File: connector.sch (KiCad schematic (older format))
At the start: 16 parts

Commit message: Add vias and ground connections
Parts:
- J301: renamed from J?; footprint (none) -> breakout:SEAM-50-02.0-S-08-2-A-K-TR
- J302: renamed from J?; footprint (none) -> breakout:SEAF-50-05.0-S-08-2-A-K-TR
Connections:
- net GND: now reaches J301.G17, J302.G17
- net GND: now also J301.A28, J301.A3, J301.A37, J301.A4, J301.A40, J301.A43, J301.B14, J301.B3, J301.B31, J301.B38, J301.B4, J301.B41, J301.B44, J301.B47, J301.C21, J301.C24, J301.C27, J301.C3, J301.C30, J301.C33, J301.C36, J301.C39, J301.C4, J301.C42, J301.C45, J301.D20, J301.D23, J301.D26, J301.D29, J301.D32, J301.D35, J301.D38, J301.D41, J301.D44, J301.E19, J301.E22, J301.E25, J301.E28, J301.E31, J301.E34, J301.E37, J301.E40, J301.E43, J301.E46, J301.F10, J301.F15, J301.F21, J301.F24, J301.F27, J301.F30, J301.F33, J301.F36, J301.F39, J301.F42, J301.F45, J301.F49, J301.G20, J301.G23, J301.G26, J301.G29, J301.G3, J301.G32, J301.G35, J301.G38, J301.G41, J301.G44, J301.G47, J301.G50, J301.H19, J301.H22, J301.H25, J301.H28, J301.H31, J301.H34, J301.H37, J301.H40, J301.H43, J301.H46, J301.H49, J302.A28, J302.A3, J302.A37, J302.A4, J302.A40, J302.A43, J302.B14, J302.B3, J302.B31, J302.B38, J302.B4, J302.B41, J302.B44, J302.B47, J302.C21, J302.C24, J302.C27, J302.C3, J302.C30, J302.C33, J302.C36, J302.C39, J302.C4, J302.C42, J302.C45, J302.D20, J302.D23, J302.D26, J302.D29, J302.D32, J302.D35, J302.D38, J302.D41, J302.D44, J302.E19, J302.E22, J302.E25, J302.E28, J302.E31, J302.E34, J302.E37, J302.E40, J302.E43, J302.E46, J302.F10, J302.F15, J302.F21, J302.F24, J302.F27, J302.F30, J302.F33, J302.F36, J302.F39, J302.F42, J302.F45, J302.F49, J302.G20, J302.G23, J302.G26, J302.G29, J302.G3, J302.G32, J302.G35, J302.G38, J302.G41, J302.G44, J302.G47, J302.G50, J302.H19, J302.H22, J302.H25, J302.H28, J302.H31, J302.H34, J302.H37, J302.H40, J302.H43, J302.H46, J302.H49
- new net: J301.C1, J302.C1
- new net: J301.C10, J302.C10
- new net: J301.C11, J302.C11
- new net: J301.C12, J302.C12
- new net: J301.C13, J302.C13
- new net: J301.C14, J302.C14
- new net: J301.C15, J302.C15
- new net: J301.C16, J302.C16
- new net: J301.C17, J302.C17
- new net: J301.C18, J302.C18
- new net: J301.C19, J302.C19
- new net: J301.C2, J302.C2
- new net: J301.C20, J302.C20
- new net: J301.C22, J302.C22
- new net: J301.C23, J302.C23
- new net: J301.C25, J302.C25
- new net: J301.C26, J302.C26
- new net: J301.C28, J302.C28
- new net: J301.C29, J302.C29
- new net: J301.C31, J302.C31
- new net: J301.C32, J302.C32
- new net: J301.C34, J302.C34
- new net: J301.C35, J302.C35
- new net: J301.C37, J302.C37
- new net: J301.C38, J302.C38
- new net: J301.C40, J302.C40
- new net: J301.C41, J302.C41
- new net: J301.C43, J302.C43
- new net: J301.C44, J302.C44
- new net: J301.C46, J302.C46
- new net: J301.C47, J302.C47
- new net: J301.C48, J302.C48
- new net: J301.C49, J302.C49
- new net: J301.C5, J302.C5
- new net: J301.C50, J302.C50
- new net: J301.C6, J302.C6
- new net: J301.C7, J302.C7
- new net: J301.C8, J302.C8
- new net: J301.C9, J302.C9
- new net: J301.D1, J302.D1
- new net: J301.D10, J302.D10
- new net: J301.D11, J302.D11
- new net: J301.D12, J302.D12
- new net: J301.D13, J302.D13
- new net: J301.D14, J302.D14
- new net: J301.D15, J302.D15
- new net: J301.D16, J302.D16
- new net: J301.D17, J302.D17
- new net: J301.D18, J302.D18
- new net: J301.D19, J302.D19
- new net: J301.D2, J302.D2
- new net: J301.D21, J302.D21
- new net: J301.D22, J302.D22
- new net: J301.D24, J302.D24
- new net: J301.D25, J302.D25
- new net: J301.D27, J302.D27
- new net: J301.D28, J302.D28
- new net: J301.D3, J302.D3
- new net: J301.D30, J302.D30
- new net: J301.D31, J302.D31
- new net: J301.D33, J302.D33
- new net: J301.D34, J302.D34
- new net: J301.D36, J302.D36
- new net: J301.D37, J302.D37
- new net: J301.D39, J302.D39
- new net: J301.D4, J302.D4
- new net: J301.D40, J302.D40
- new net: J301.D42, J302.D42
- new net: J301.D43, J302.D43
- new net: J301.D45, J302.D45
- new net: J301.D46, J302.D46
- new net: J301.D47, J302.D47
- new net: J301.D48, J302.D48
- new net: J301.D49, J302.D49
- new net: J301.D5, J302.D5
- new net: J301.D50, J302.D50
- new net: J301.D6, J302.D6
- new net: J301.D7, J302.D7
- new net: J301.D8, J302.D8
- new net: J301.D9, J302.D9
- new net: J301.A1, J302.A1
- new net: J301.A10, J302.A10
- new net: J301.A11, J302.A11
- new net: J301.A12, J302.A12
- new net: J301.A13, J302.A13
- new net: J301.A14, J302.A14
- new net: J301.A15, J302.A15
- new net: J301.A16, J302.A16
- new net: J301.A17, J302.A17
- new net: J301.A18, J302.A18
- new net: J301.A19, J302.A19
- new net: J301.A2, J302.A2
- new net: J301.A20, J302.A20
- new net: J301.A21, J302.A21
- new net: J301.A22, J302.A22
- new net: J301.A23, J302.A23
- new net: J301.A24, J302.A24
- new net: J301.A25, J302.A25
- new net: J301.A26, J302.A26
- new net: J301.A27, J302.A27
- new net: J301.A29, J302.A29
- new net: J301.A30, J302.A30
- new net: J301.A31, J302.A31
- new net: J301.A32, J302.A32
- new net: J301.A33, J302.A33
- new net: J301.A34, J302.A34
- new net: J301.A35, J302.A35
- new net: J301.A36, J302.A36
- new net: J301.A38, J302.A38
- new net: J301.A39, J302.A39
- new net: J301.A41, J302.A41
- new net: J301.A42, J302.A42
- new net: J301.A44, J302.A44
- new net: J301.A45, J302.A45
- new net: J301.A46, J302.A46
- new net: J301.A47, J302.A47
- new net: J301.A48, J302.A48
- new net: J301.A49, J302.A49
- new net: J301.A5, J302.A5
- new net: J301.A50, J302.A50
- new net: J301.A6, J302.A6
- new net: J301.A7, J302.A7
- new net: J301.A8, J302.A8
- new net: J301.A9, J302.A9
- new net: J301.B1, J302.B1
- new net: J301.B10, J302.B10
- new net: J301.B11, J302.B11
- new net: J301.B12, J302.B12
- new net: J301.B13, J302.B13
- new net: J301.B15, J302.B15
- new net: J301.B16, J302.B16
- new net: J301.B17, J302.B17
- new net: J301.B18, J302.B18
- new net: J301.B19, J302.B19
- new net: J301.B2, J302.B2
- new net: J301.B20, J302.B20
- new net: J301.B21, J302.B21
- new net: J301.B22, J302.B22
- new net: J301.B23, J302.B23
- new net: J301.B24, J302.B24
- new net: J301.B25, J302.B25
- new net: J301.B26, J302.B26
- new net: J301.B27, J302.B27
- new net: J301.B28, J302.B28
- new net: J301.B29, J302.B29
- new net: J301.B30, J302.B30
- new net: J301.B32, J302.B32
- new net: J301.B33, J302.B33
- new net: J301.B34, J302.B34
- new net: J301.B35, J302.B35
- new net: J301.B36, J302.B36
- new net: J301.B37, J302.B37
- new net: J301.B39, J302.B39
- new net: J301.B40, J302.B40
- new net: J301.B42, J302.B42
- new net: J301.B43, J302.B43
- new net: J301.B45, J302.B45
- new net: J301.B46, J302.B46
- new net: J301.B48, J302.B48
- new net: J301.B49, J302.B49
- new net: J301.B5, J302.B5
- new net: J301.B50, J302.B50
- new net: J301.B6, J302.B6
- new net: J301.B7, J302.B7
- new net: J301.B8, J302.B8
- new net: J301.B9, J302.B9
- new net: J301.F1, J302.F1
- new net: J301.F11, J302.F11
- new net: J301.F12, J302.F12
- new net: J301.F13, J302.F13
- new net: J301.F14, J302.F14
- new net: J301.F16, J302.F16
- new net: J301.F17, J302.F17
- new net: J301.F18, J302.F18
- new net: J301.F19, J302.F19
- new net: J301.F2, J302.F2
- new net: J301.F20, J302.F20
- new net: J301.F22, J302.F22
- new net: J301.F23, J302.F23
- new net: J301.F25, J302.F25
- new net: J301.F26, J302.F26
- new net: J301.F28, J302.F28
- new net: J301.F29, J302.F29
- new net: J301.F3, J302.F3
- new net: J301.F31, J302.F31
- new net: J301.F32, J302.F32
- new net: J301.F34, J302.F34
- new net: J301.F35, J302.F35
- new net: J301.F37, J302.F37
- new net: J301.F38, J302.F38
- new net: J301.F4, J302.F4
- new net: J301.F40, J302.F40
- new net: J301.F41, J302.F41
- new net: J301.F43, J302.F43
- new net: J301.F44, J302.F44
- new net: J301.F46, J302.F46
- new net: J301.F47, J302.F47
- new net: J301.F48, J302.F48
- new net: J301.F5, J302.F5
- new net: J301.F50, J302.F50
- new net: J301.F6, J302.F6
- new net: J301.F7, J302.F7
- new net: J301.F8, J302.F8
- new net: J301.F9, J302.F9
- new net: J301.H1, J302.H1
- new net: J301.H10, J302.H10
- new net: J301.H11, J302.H11
- new net: J301.H12, J302.H12
- new net: J301.H13, J302.H13
- new net: J301.H14, J302.H14
- new net: J301.H15, J302.H15
- new net: J301.H16, J302.H16
- new net: J301.H17, J302.H17
- new net: J301.H18, J302.H18
- new net: J301.H2, J302.H2
- new net: J301.H20, J302.H20
- new net: J301.H21, J302.H21
- new net: J301.H23, J302.H23
- new net: J301.H24, J302.H24
- new net: J301.H26, J302.H26
- new net: J301.H27, J302.H27
- new net: J301.H29, J302.H29
- new net: J301.H3, J302.H3
- new net: J301.H30, J302.H30
- new net: J301.H32, J302.H32
- new net: J301.H33, J302.H33
- new net: J301.H35, J302.H35
- new net: J301.H36, J302.H36
- new net: J301.H38, J302.H38
- new net: J301.H39, J302.H39
- new net: J301.H4, J302.H4
- new net: J301.H41, J302.H41
- new net: J301.H42, J302.H42
- new net: J301.H44, J302.H44
- new net: J301.H45, J302.H45
- new net: J301.H47, J302.H47
- new net: J301.H48, J302.H48
- new net: J301.H5, J302.H5
- new net: J301.H50, J302.H50
- new net: J301.H6, J302.H6
- new net: J301.H7, J302.H7
- new net: J301.H8, J302.H8
- new net: J301.H9, J302.H9
- new net: J301.E1, J302.E1
- new net: J301.E10, J302.E10
- new net: J301.E11, J302.E11
- new net: J301.E12, J302.E12
- new net: J301.E13, J302.E13
- new net: J301.E14, J302.E14
- new net: J301.E15, J302.E15
- new net: J301.E16, J302.E16
- new net: J301.E17, J302.E17
- new net: J301.E18, J302.E18
- new net: J301.E2, J302.E2
- new net: J301.E20, J302.E20
- new net: J301.E21, J302.E21
- new net: J301.E23, J302.E23
- new net: J301.E24, J302.E24
- new net: J301.E26, J302.E26
- new net: J301.E27, J302.E27
- new net: J301.E29, J302.E29
- new net: J301.E3, J302.E3
- new net: J301.E30, J302.E30
- new net: J301.E32, J302.E32
- new net: J301.E33, J302.E33
- new net: J301.E35, J302.E35
- new net: J301.E36, J302.E36
- new net: J301.E38, J302.E38
- new net: J301.E39, J302.E39
- new net: J301.E4, J302.E4
- new net: J301.E41, J302.E41
- new net: J301.E42, J302.E42
- new net: J301.E44, J302.E44
- new net: J301.E45, J302.E45
- new net: J301.E47, J302.E47
- new net: J301.E48, J302.E48
- new net: J301.E49, J302.E49
- new net: J301.E5, J302.E5
- new net: J301.E50, J302.E50
- new net: J301.E6, J302.E6
- new net: J301.E7, J302.E7
- new net: J301.E8, J302.E8
- new net: J301.E9, J302.E9
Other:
- moved on the sheet: J301G, J302G

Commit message: Add hierarchial pins for CAN, TODO regen netlist
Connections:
- net CAN0_TX: now reaches J301.D18, J302.D18
- net CAN0_RX: now reaches J301.D19, J302.D19
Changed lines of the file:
@@
 $EndComp
 $Comp
-L GND #PWR06
+L GND #PWR302
 U 1 1 5A131DD5
 P 2520 5900
-F 0 "#PWR06" H 2520 5650 50  0001 C CNN
+F 0 "#PWR302" H 2520 5650 50  0001 C CNN
 F 1 "GND" H 2520 5750 50  0000 C CNN
 F 2 "" H 2520 5900 50  0001 C CNN
@@
 $EndComp
 $Comp
-L GND #PWR?
+L GND #PWR303
 U 1 1 5A135532
 P 6690 5990
-F 0 "#PWR?" H 6690 5740 50  0001 C CNN
+F 0 "#PWR303" H 6690 5740 50  0001 C CNN
 F 1 "GND" H 6690 5840 50  0000 C CNN
 F 2 "" H 6690 5990 50  0001 C CNN
@@
 $EndComp
 $Comp
-L GND #PWR?
+L GND #PWR301
 U 1 1 5A136A81
 P 11920 5850
-F 0 "#PWR?" H 11920 5600 50  0001 C CNN
+F 0 "#PWR301" H 11920 5600 50  0001 C CNN
 F 1 "GND" H 11920 5700 50  0000 C CNN
 F 2 "" H 11920 5850 50  0001 C CNN
@@
 $EndComp
 $Comp
-L GND #PWR?
+L GND #PWR304
 U 1 1 5A1388D0
 P 17610 6150
-F 0 "#PWR?" H 17610 5900 50  0001 C CNN
+F 0 "#PWR304" H 17610 5900 50  0001 C CNN
 F 1 "GND" H 17610 6000 50  0000 C CNN
 F 2 "" H 17610 6150 50  0001 C CNN
@@
 $EndComp
 $Comp
-L GND #PWR?
+L GND #PWR305
 U 1 1 5A13A931
 P 2690 13040
-F 0 "#PWR?" H 2690 12790 50  0001 C CNN
+F 0 "#PWR305" H 2690 12790 50  0001 C CNN
 F 1 "GND" H 2690 12890 50  0000 C CNN
 F 2 "" H 2690 13040 50  0001 C CNN
@@
 $EndComp
 $Comp
-L GND #PWR?
+L GND #PWR307
 U 1 1 5A13C2DB
 P 6710 13120
-F 0 "#PWR?" H 6710 12870 50  0001 C CNN
+F 0 "#PWR307" H 6710 12870 50  0001 C CNN
 F 1 "GND" H 6710 12970 50  0000 C CNN
 F 2 "" H 6710 13120 50  0001 C CNN
@@
 Connection ~ 6710 9520
 $Comp
-L GND #PWR?
+L GND #PWR306
 U 1 1 5A13E42C
 P 11730 13050
-F 0 "#PWR?" H 11730 12800 50  0001 C CNN
+F 0 "#PWR306" H 11730 12800 50  0001 C CNN
 F 1 "GND" H 11730 12900 50  0000 C CNN
 F 2 "" H 11730 13050 50  0001 C CNN
@@
 Connection ~ 11730 8190
 $Comp
-L GND #PWR?
+L GND #PWR308
 U 1 1 5A140DD2
 P 17670 13270
-F 0 "#PWR?" H 17670 13020 50  0001 C CNN
+F 0 "#PWR308" H 17670 13020 50  0001 C CNN
 F 1 "GND" H 17670 13120 50  0000 C CNN
 F 2 "" H 17670 13270 50  0001 C CNN
@@
 Connection ~ 17670 10340
 Connection ~ 17670 10040
+Text HLabel 19210 580  2    60   Input ~ 0
+CAN0_TX
+Text HLabel 19210 710  2    60   Input ~ 0
+CAN0_RX
+Wire Wire Line
+	17820 2700 17820 710
+Wire Wire Line
+	17820 710  19210 710
+Connection ~ 17820 2700
+Wire Wire Line
+	19210 580  17750 580
+Wire Wire Line
+	17750 580  17750 2600
+Connection ~ 17750 2600
 $EndSCHEMATC

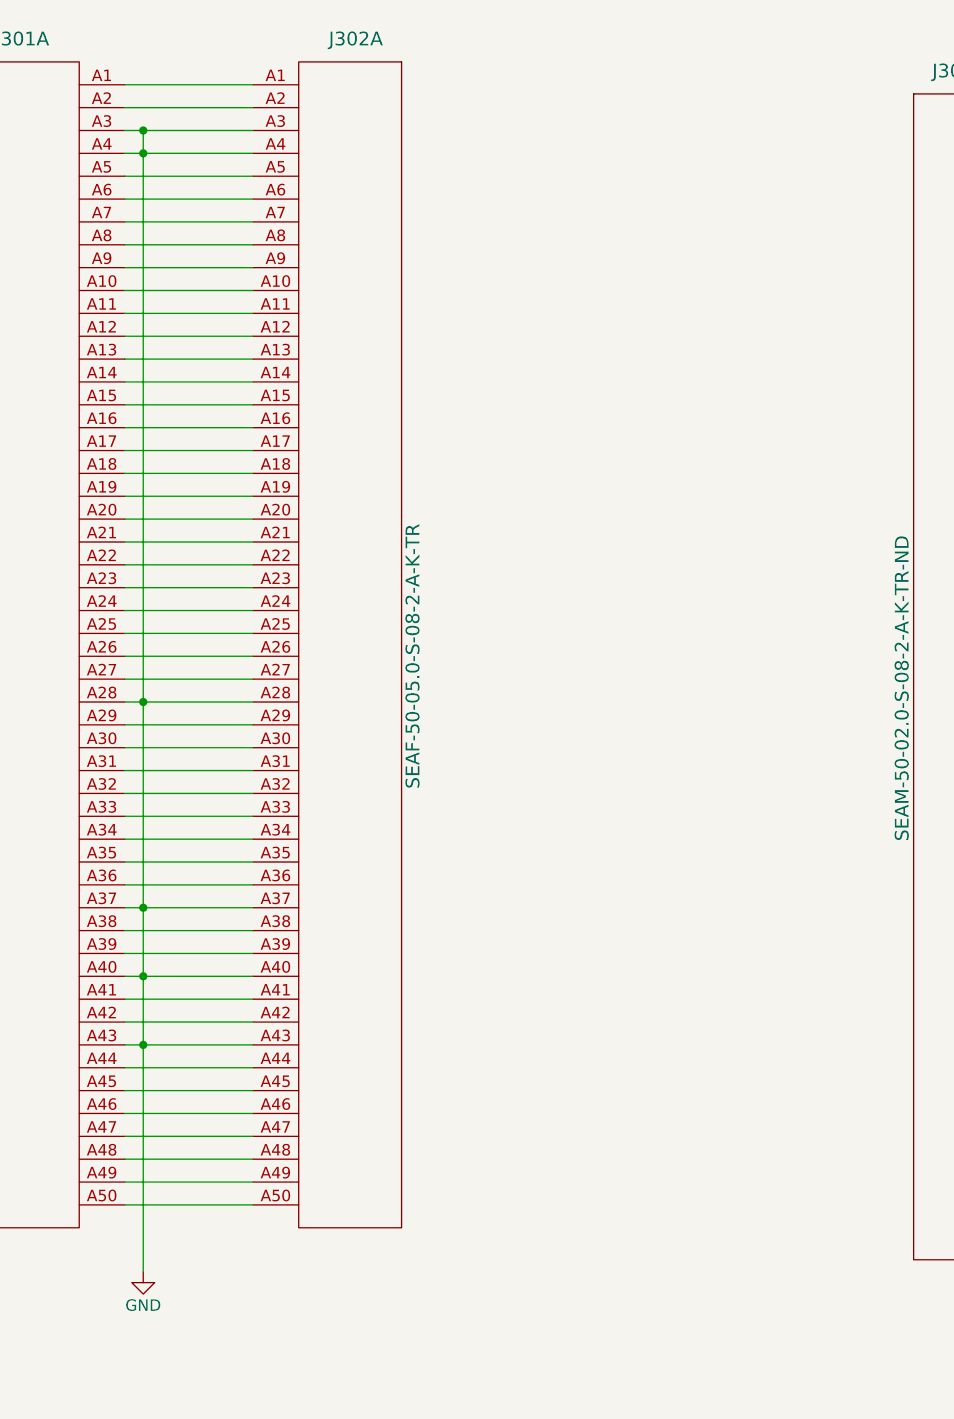
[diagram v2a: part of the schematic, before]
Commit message: Add some protection diodes, connect most things up TODO add TVS diodes to CAN bus terinals
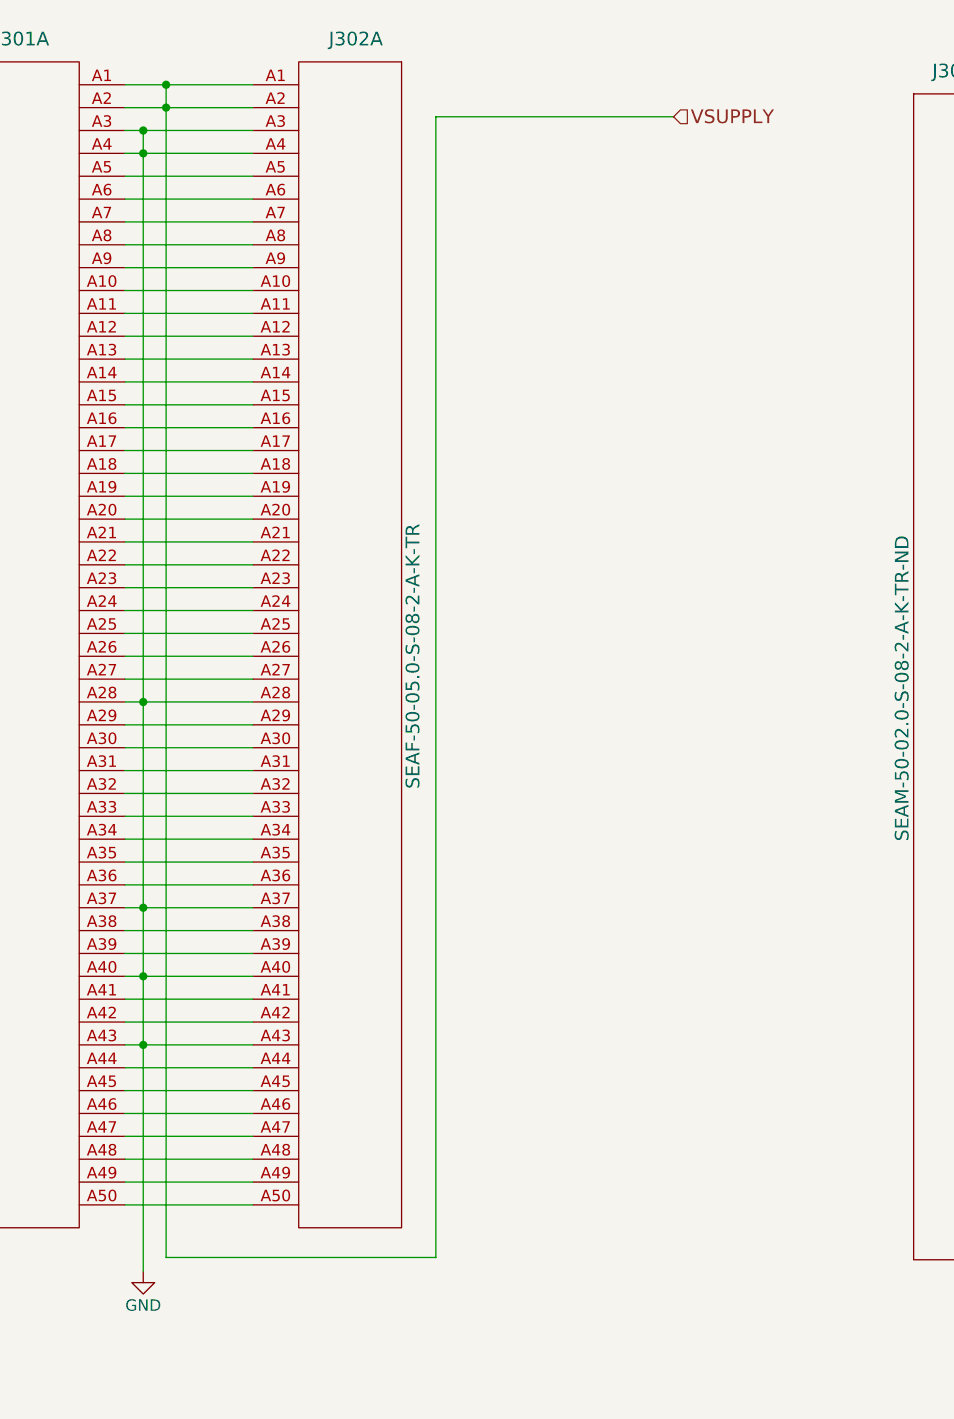
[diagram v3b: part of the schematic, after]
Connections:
- net VSUPPLY: now reaches J301.A1, J302.A1
- net VSUPPLY: now also J301.A2, J302.A2
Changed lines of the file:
@@
 LIBS:sn65hvd256
 LIBS:samtec
+LIBS:mic5365-33yd5-tr
 LIBS:can-breakout-cache
 EELAYER 25 0
@@
 	17750 580  17750 2600
 Connection ~ 17750 2600
+Text HLabel 4840 850  2    60   Input ~ 0
+VSUPPLY
+Wire Wire Line
+	4840 850  3800 850
+Wire Wire Line
+	3800 850  3800 5840
+Wire Wire Line
+	3800 5840 2620 5840
+Wire Wire Line
+	2620 5840 2620 710
+Connection ~ 2620 710
+Connection ~ 2620 810
 $EndSCHEMATC

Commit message: Parts laid out, only routing left
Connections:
- net GND: now also J301.A3, J301.A4, J301.B3, J301.B4, J302.A3, J302.A4, J302.B3, J302.B4; no longer J301.A28, J301.A3, J301.A37, J301.A4, J301.A40, J301.A43, J301.B14, J301.B3, J301.B31, J301.B38, J301.B4, J301.B41, J301.B44, J301.B47, J301.C21, J301.C24, J301.C27, J301.C3, J301.C30, J301.C33, J301.C36, J301.C39, J301.C4, J301.C42, J301.C45, J301.D20, J301.D23, J301.D26, J301.D29, J301.D32, J301.D35, J301.D38, J301.D41, J301.D44, J301.E19, J301.E22, J301.E25, J301.E28, J301.E31, J301.E34, J301.E37, J301.E40, J301.E43, J301.E46, J301.F10, J301.F15, J301.F21, J301.F24, J301.F27, J301.F30, J301.F33, J301.F36, J301.F39, J301.F42, J301.F45, J301.F49, J301.G17, J301.G20, J301.G23, J301.G26, J301.G29, J301.G3, J301.G32, J301.G35, J301.G38, J301.G41, J301.G44, J301.G47, J301.G50, J301.H19, J301.H22, J301.H25, J301.H28, J301.H31, J301.H34, J301.H37, J301.H40, J301.H43, J301.H46, J301.H49, J302.A28, J302.A3, J302.A37, J302.A4, J302.A40, J302.A43, J302.B14, J302.B3, J302.B31, J302.B38, J302.B4, J302.B41, J302.B44, J302.B47, J302.C21, J302.C24, J302.C27, J302.C3, J302.C30, J302.C33, J302.C36, J302.C39, J302.C4, J302.C42, J302.C45, J302.D20, J302.D23, J302.D26, J302.D29, J302.D32, J302.D35, J302.D38, J302.D41, J302.D44, J302.E19, J302.E22, J302.E25, J302.E28, J302.E31, J302.E34, J302.E37, J302.E40, J302.E43, J302.E46, J302.F10, J302.F15, J302.F21, J302.F24, J302.F27, J302.F30, J302.F33, J302.F36, J302.F39, J302.F42, J302.F45, J302.F49, J302.G17, J302.G20, J302.G23, J302.G26, J302.G29, J302.G3, J302.G32, J302.G35, J302.G38, J302.G41, J302.G44, J302.G47, J302.G50, J302.H19, J302.H22, J302.H25, J302.H28, J302.H31, J302.H34, J302.H37, J302.H40, J302.H43, J302.H46, J302.H49
- net VSUPPLY: now also J301.A1, J301.A2, J301.B1, J301.B2, J301.C1, J301.C2, J302.A1, J302.A2, J302.B1, J302.B2, J302.C1, J302.C2; no longer J301.A1, J301.A2, J302.A1, J302.A2
- net CAN1_RX: now reaches J301.D17, J302.D17
- new net: J301.A10, J302.A10
- new net: J301.A11, J302.A11
- new net: J301.A12, J302.A12
- new net: J301.A13, J302.A13
- new net: J301.A14, J302.A14
- new net: J301.A15, J302.A15
- new net: J301.A16, J302.A16
- new net: J301.A17, J302.A17
- new net: J301.A18, J302.A18
- new net: J301.A19, J302.A19
- new net: J301.A20, J302.A20
- new net: J301.A21, J302.A21
- new net: J301.A22, J302.A22
- new net: J301.A23, J302.A23
- new net: J301.A24, J302.A24
- new net: J301.A25, J302.A25
- new net: J301.A26, J302.A26
- new net: J301.A27, J302.A27
- new net: J301.A28, J302.A28
- new net: J301.A29, J302.A29
- new net: J301.A30, J302.A30
- new net: J301.A31, J302.A31
- new net: J301.A32, J302.A32
- new net: J301.A33, J302.A33
- new net: J301.A34, J302.A34
- new net: J301.A35, J302.A35
- new net: J301.A36, J302.A36
- new net: J301.A37, J302.A37
- new net: J301.A38, J302.A38
- new net: J301.A39, J302.A39
- new net: J301.A40, J302.A40
- new net: J301.A41, J302.A41
- new net: J301.A42, J302.A42
- new net: J301.A43, J302.A43
- new net: J301.A44, J302.A44
- new net: J301.A45, J302.A45
- new net: J301.A46, J302.A46
- new net: J301.A47, J302.A47
- new net: J301.A48, J302.A48
- new net: J301.A49, J302.A49
- new net: J301.A5, J302.A5
- new net: J301.A50, J302.A50
- new net: J301.A6, J302.A6
- new net: J301.A7, J302.A7
- new net: J301.A8, J302.A8
- new net: J301.A9, J302.A9
- new net: J301.D20, J302.D20
- new net: J301.D23, J302.D23
- new net: J301.D26, J302.D26
- new net: J301.D29, J302.D29
- new net: J301.D32, J302.D32
- new net: J301.D35, J302.D35
- new net: J301.D38, J302.D38
- new net: J301.D41, J302.D41
- new net: J301.D44, J302.D44
- new net: J301.B10, J302.B10
- new net: J301.B11, J302.B11
- new net: J301.B12, J302.B12
- new net: J301.B13, J302.B13
- new net: J301.B14, J302.B14
- new net: J301.B15, J302.B15
- new net: J301.B16, J302.B16
- new net: J301.B17, J302.B17
- new net: J301.B18, J302.B18
- new net: J301.B19, J302.B19
- new net: J301.B20, J302.B20
- new net: J301.B21, J302.B21
- new net: J301.B22, J302.B22
- new net: J301.B23, J302.B23
- new net: J301.B24, J302.B24
- new net: J301.B25, J302.B25
- new net: J301.B26, J302.B26
- new net: J301.B27, J302.B27
- new net: J301.B28, J302.B28
- new net: J301.B29, J302.B29
- new net: J301.B30, J302.B30
- new net: J301.B31, J302.B31
- new net: J301.B32, J302.B32
- new net: J301.B33, J302.B33
- new net: J301.B34, J302.B34
- new net: J301.B35, J302.B35
- new net: J301.B36, J302.B36
- new net: J301.B37, J302.B37
- new net: J301.B38, J302.B38
- new net: J301.B39, J302.B39
- new net: J301.B40, J302.B40
- new net: J301.B41, J302.B41
- new net: J301.B42, J302.B42
- new net: J301.B43, J302.B43
- new net: J301.B44, J302.B44
- new net: J301.B45, J302.B45
- new net: J301.B46, J302.B46
- new net: J301.B47, J302.B47
- new net: J301.B48, J302.B48
- new net: J301.B49, J302.B49
- new net: J301.B5, J302.B5
- new net: J301.B50, J302.B50
- new net: J301.B6, J302.B6
- new net: J301.B7, J302.B7
- new net: J301.B8, J302.B8
- new net: J301.B9, J302.B9
- new net: J301.C10, J302.C10
- new net: J301.C11, J302.C11
- new net: J301.C12, J302.C12
- new net: J301.C13, J302.C13
- new net: J301.C14, J302.C14
- new net: J301.C15, J302.C15
- new net: J301.C16, J302.C16
- new net: J301.C17, J302.C17
- new net: J301.C19, J302.C19
- new net: J301.C20, J302.C20
- new net: J301.C21, J302.C21
- new net: J301.C22, J302.C22
- new net: J301.C23, J302.C23
- new net: J301.C24, J302.C24
- new net: J301.C25, J302.C25
- new net: J301.C26, J302.C26
- new net: J301.C27, J302.C27
- new net: J301.C28, J302.C28
- new net: J301.C29, J302.C29
- new net: J301.C3, J301.C4, J302.C3, J302.C4
- new net: J301.C30, J302.C30
- new net: J301.C31, J302.C31
- new net: J301.C32, J302.C32
- new net: J301.C33, J302.C33
- new net: J301.C34, J302.C34
- new net: J301.C35, J302.C35
- new net: J301.C36, J302.C36
- new net: J301.C37, J302.C37
- new net: J301.C38, J302.C38
- new net: J301.C39, J302.C39
- new net: J301.C40, J302.C40
- new net: J301.C41, J302.C41
- new net: J301.C42, J302.C42
- new net: J301.C43, J302.C43
- new net: J301.C44, J302.C44
- new net: J301.C45, J302.C45
- new net: J301.C46, J302.C46
- new net: J301.C47, J302.C47
- new net: J301.C48, J302.C48
- new net: J301.C49, J302.C49
- new net: J301.C5, J302.C5
- new net: J301.C50, J302.C50
- new net: J301.C6, J302.C6
- new net: J301.C7, J302.C7
- new net: J301.C8, J302.C8
- new net: J301.C9, J302.C9
- new net: J301.G1, J302.G1
- new net: J301.G10, J302.G10
- new net: J301.G11, J302.G11
- new net: J301.G12, J302.G12
- new net: J301.G13, J302.G13
- new net: J301.G14, J302.G14
- new net: J301.G15, J302.G15
- new net: J301.G16, J302.G16
- new net: J301.G17, J302.G17
- new net: J301.G18, J302.G18
- new net: J301.G19, J302.G19
- new net: J301.G2, J302.G2
- new net: J301.G20, J302.G20
- new net: J301.G21, J302.G21
- new net: J301.G22, J302.G22
- new net: J301.G23, J302.G23
- new net: J301.G24, J302.G24
- new net: J301.G25, J302.G25
- new net: J301.G26, J302.G26
- new net: J301.G27, J302.G27
- new net: J301.G28, J302.G28
- new net: J301.G29, J302.G29
- new net: J301.G3, J302.G3
- new net: J301.G30, J302.G30
- new net: J301.G31, J302.G31
- new net: J301.G32, J302.G32
- new net: J301.G33, J302.G33
- new net: J301.G34, J302.G34
- new net: J301.G35, J302.G35
- new net: J301.G36, J302.G36
- new net: J301.G37, J302.G37
- new net: J301.G38, J302.G38
- new net: J301.G39, J302.G39
- new net: J301.G4, J302.G4
- new net: J301.G40, J302.G40
- new net: J301.G41, J302.G41
- new net: J301.G42, J302.G42
- new net: J301.G43, J302.G43
- new net: J301.G44, J302.G44
- new net: J301.G45, J302.G45
- new net: J301.G46, J302.G46
- new net: J301.G47, J302.G47
- new net: J301.G48, J302.G48
- new net: J301.G49, J302.G49
- new net: J301.G5, J302.G5
- new net: J301.G50, J302.G50
- new net: J301.G6, J302.G6
- new net: J301.G7, J302.G7
- new net: J301.G8, J302.G8
- new net: J301.G9, J302.G9
- new net: J301.H19, J302.H19
- new net: J301.H22, J302.H22
- new net: J301.H25, J302.H25
- new net: J301.H28, J302.H28
- new net: J301.H31, J302.H31
- new net: J301.H34, J302.H34
- new net: J301.H37, J302.H37
- new net: J301.H40, J302.H40
- new net: J301.H43, J302.H43
- new net: J301.H46, J302.H46
- new net: J301.H49, J302.H49
- new net: J301.F1, J302.F1
- new net: J301.F10, J302.F10
- new net: J301.F11, J302.F11
- new net: J301.F12, J302.F12
- new net: J301.F13, J302.F13
- new net: J301.F14, J302.F14
- new net: J301.F15, J302.F15
- new net: J301.F16, J302.F16
- new net: J301.F17, J302.F17
- new net: J301.F18, J302.F18
- new net: J301.F19, J302.F19
- new net: J301.F2, J302.F2
- new net: J301.F20, J302.F20
- new net: J301.F21, J302.F21
- new net: J301.F22, J302.F22
- new net: J301.F23, J302.F23
- new net: J301.F24, J302.F24
- new net: J301.F25, J302.F25
- new net: J301.F26, J302.F26
- new net: J301.F27, J302.F27
- new net: J301.F28, J302.F28
- new net: J301.F29, J302.F29
- new net: J301.F3, J302.F3
- new net: J301.F30, J302.F30
- new net: J301.F31, J302.F31
- new net: J301.F32, J302.F32
- new net: J301.F33, J302.F33
- new net: J301.F34, J302.F34
- new net: J301.F35, J302.F35
- new net: J301.F36, J302.F36
- new net: J301.F37, J302.F37
- new net: J301.F38, J302.F38
- new net: J301.F39, J302.F39
- new net: J301.F4, J302.F4
- new net: J301.F40, J302.F40
- new net: J301.F41, J302.F41
- new net: J301.F42, J302.F42
- new net: J301.F43, J302.F43
- new net: J301.F44, J302.F44
- new net: J301.F45, J302.F45
- new net: J301.F46, J302.F46
- new net: J301.F47, J302.F47
- new net: J301.F48, J302.F48
- new net: J301.F49, J302.F49
- new net: J301.F5, J302.F5
- new net: J301.F50, J302.F50
- new net: J301.F6, J302.F6
- new net: J301.F7, J302.F7
- new net: J301.F8, J302.F8
- new net: J301.F9, J302.F9
- new net: J301.E19, J302.E19
- new net: J301.E22, J302.E22
- new net: J301.E25, J302.E25
- new net: J301.E28, J302.E28
- new net: J301.E31, J302.E31
- new net: J301.E34, J302.E34
- new net: J301.E37, J302.E37
- new net: J301.E40, J302.E40
- new net: J301.E43, J302.E43
- new net: J301.E46, J302.E46
- new net CAN1_TX: J301.C18, J302.C18

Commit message: Finish layout and generate Gerber files
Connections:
- net GND: now also J301.C3, J301.C4, J302.C3, J302.C4
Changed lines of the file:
@@
 L GND #PWR018
 U 1 1 5A56619A
-P 11920 6560
-F 0 "#PWR018" H 11920 6310 50  0001 C CNN
-F 1 "GND" H 11920 6410 50  0000 C CNN
-F 2 "" H 11920 6560 50  0001 C CNN
-F 3 "" H 11920 6560 50  0001 C CNN
-	1    11920 6560
+P 11920 6570
+F 0 "#PWR018" H 11920 6320 50  0001 C CNN
+F 1 "GND" H 11920 6420 50  0000 C CNN
+F 2 "" H 11920 6570 50  0001 C CNN
+F 3 "" H 11920 6570 50  0001 C CNN
+	1    11920 6570
 	1    0    0    -1
 $EndComp
